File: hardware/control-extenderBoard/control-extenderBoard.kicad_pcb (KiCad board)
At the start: 2 copper layers, 100 x 135 mm, 88 parts, among them J1 12V + GND (TP), J10 SCL6 + GND (TP), J11 SDA6 + GND (TP), J12 3V3 + GND (TP), J13 12V + GND (TP), J14 SCL6 + GND (TP), J15 SDA6 + GND (TP), J17 24V IN, J18 GND, J2 12V Out, J3 5V out, J4 3V3 + GND (TP), J5 GND, J6 SCL7 Differential (TP), J7 SDA7 Differential (TP), J8 RS485, J9 3V3 out, P1 ISP, U1 MAX3485, U10 LM2576T-12, U11 ICM-426XX_Breakout, U2 PCA9600D, U3 TCA9548A_1-to-8_I2C_Multiplex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, U4 LM2576T-3.3, U5 PCA9600D, U6 PCA82C251, U7 PCA82C251, U8 PCA9600D, U9 LM2576T-5

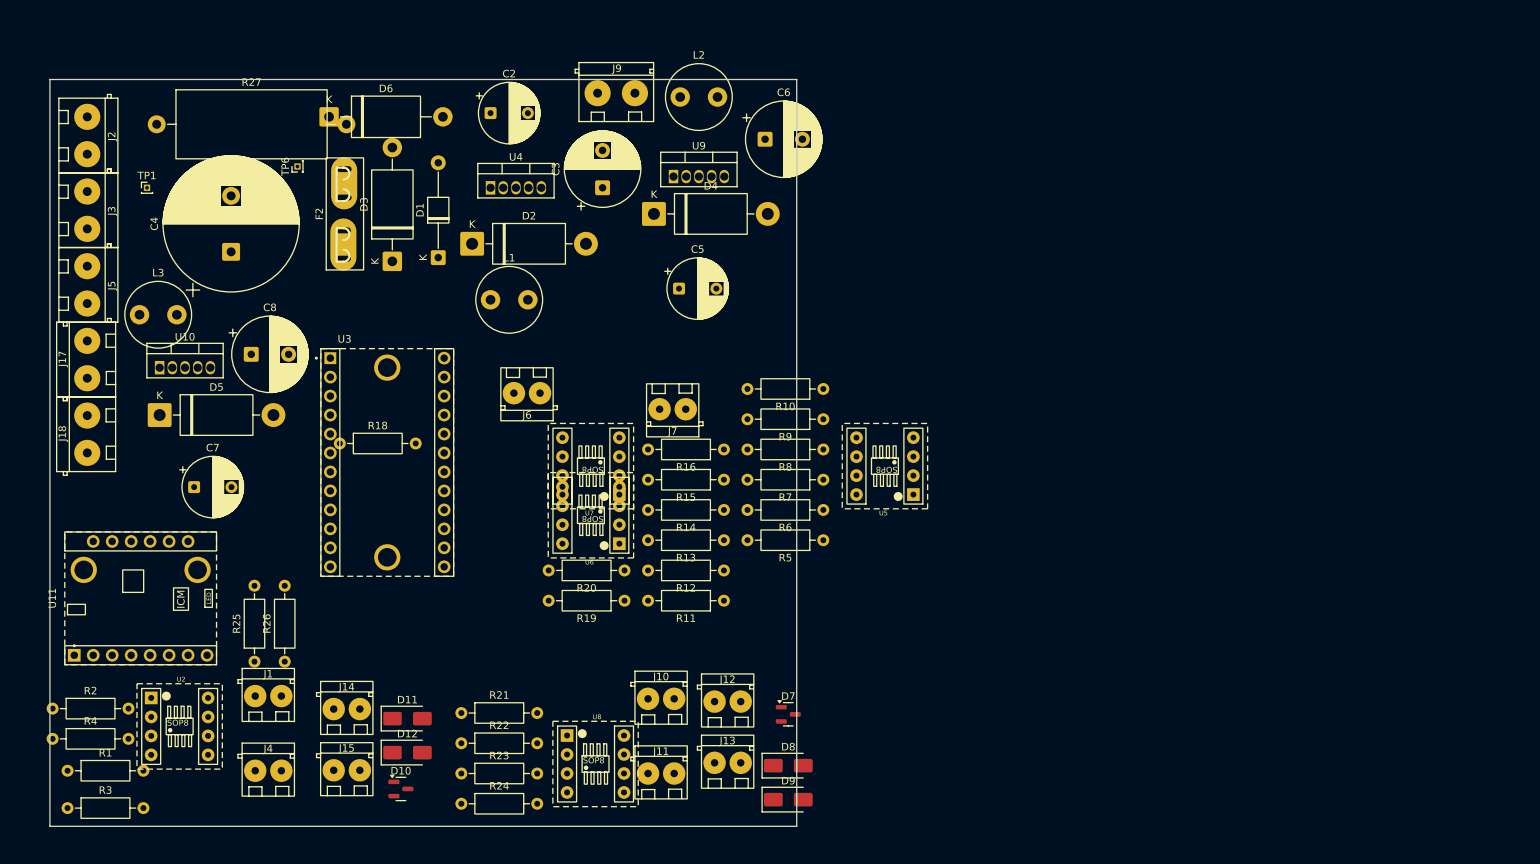
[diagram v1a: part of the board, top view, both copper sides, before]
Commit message: extenderBoard: Add remote encoder board, start arranging
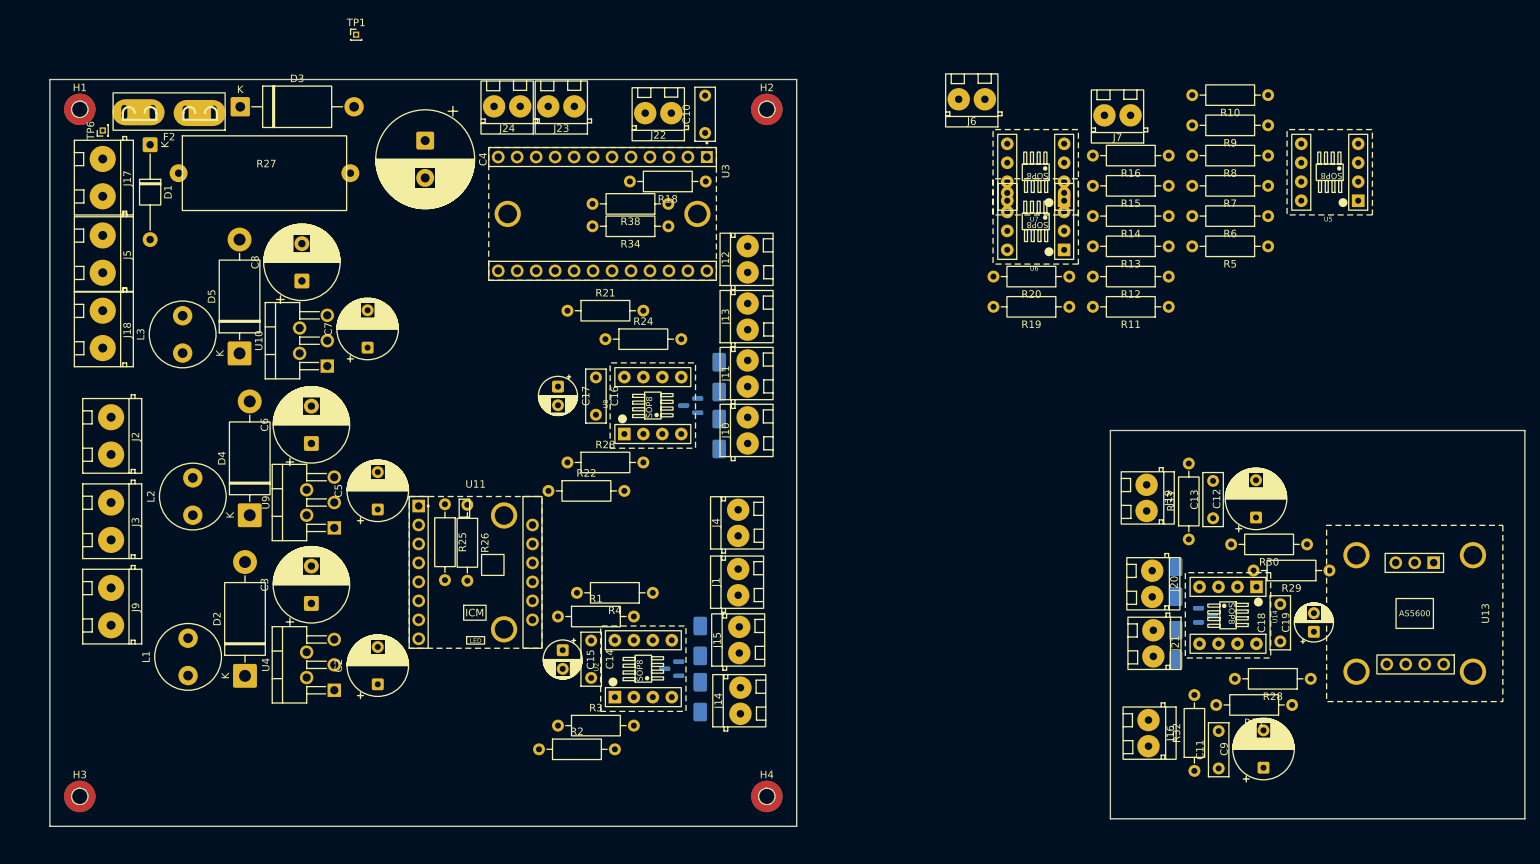
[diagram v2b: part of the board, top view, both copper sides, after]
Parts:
- removed D6: TVS 40V, Diode_THT:D_DO-201AE_P15.24mm_Horizontal
- added C10: 100n, Capacitor_THT:C_Disc_D7.0mm_W2.5mm_P5.00mm, F.Cu at (132.7, 37.2)
- added C11: 100n, Capacitor_THT:C_Disc_D7.0mm_W2.5mm_P5.00mm, F.Cu at (201.5, 122.2)
- added C12: 100u, Capacitor_THT:CP_Radial_D8.0mm_P5.00mm, F.Cu at (206.5, 88.7)
- added C13: 100n, Capacitor_THT:C_Disc_D7.0mm_W2.5mm_P5.00mm, F.Cu at (200.8, 88.8)
- added C14: 100n, Capacitor_THT:C_Disc_D7.0mm_W2.5mm_P5.00mm, F.Cu at (117.5, 105.1)
- added C15: 10uf, Capacitor_THT:CP_Radial_D5.0mm_P2.50mm, F.Cu at (113.7, 106.4)
- added C16: 100n, Capacitor_THT:C_Disc_D7.0mm_W2.5mm_P5.00mm, F.Cu at (118.1, 69.9)
- added C17: 10uf, Capacitor_THT:CP_Radial_D5.0mm_P2.50mm, F.Cu at (113.0, 71.1)
- added C18: 100n, Capacitor_THT:C_Disc_D7.0mm_W2.5mm_P5.00mm, F.Cu at (209.8, 105.2)
- added C19: 10uf, Capacitor_THT:CP_Radial_D5.0mm_P2.50mm, F.Cu at (214.2, 104.0)
- added C9: 100u, Capacitor_THT:CP_Radial_D8.0mm_P5.00mm, F.Cu at (207.5, 122.2)
- added D14: BAT54A, Package_TO_SOT_SMD:SOT-23, B.Cu at (199.8, 101.8)
- added D15: SMAJ150A, Diode_SMD:D_SMA, B.Cu at (195.8, 105.8)
- added D16: SMAJ150A, Diode_SMD:D_SMA, B.Cu at (195.8, 97.2)
- added H1: MountingHole_Pad, mountingHoles_libJonny:MountingHole_2.2mm_NPTH-with-pad_DRC-clearance-error, F.Cu at (49.0, 34.0)
- added H2: MountingHole_Pad, mountingHoles_libJonny:MountingHole_2.2mm_NPTH-with-pad_DRC-clearance-error, F.Cu at (141.0, 34.0)
- added H3: MountingHole_Pad, mountingHoles_libJonny:MountingHole_2.2mm_NPTH-with-pad_DRC-clearance-error, F.Cu at (49.0, 126.0)
- added H4: MountingHole_Pad, mountingHoles_libJonny:MountingHole_2.2mm_NPTH-with-pad_DRC-clearance-error, F.Cu at (141.0, 126.0)
- added J16: 12V + GND (TP), terminals_libJonny:ScrewTerminal_P3.5mm_2Pin_FP7x7, F.Cu at (192.1, 115.8)
- added J19: 3V3 + GND (TP), terminals_libJonny:ScrewTerminal_P3.5mm_2Pin_FP7x7, F.Cu at (191.8, 84.3)
- added J20: SCL6 + GND (TP), terminals_libJonny:ScrewTerminal_P3.5mm_2Pin_FP7x7, F.Cu at (192.6, 95.8)
- added J21: SDA6 + GND (TP), terminals_libJonny:ScrewTerminal_P3.5mm_2Pin_FP7x7, F.Cu at (192.8, 103.8)
- added J22: SDA, SCL - ESP32, terminals_libJonny:ScrewTerminal_P3.5mm_2Pin_FP7x7, F.Cu at (128.2, 34.5)
- added J23: I2C Reserve, terminals_libJonny:ScrewTerminal_P3.5mm_2Pin_FP7x7, F.Cu at (115.2, 33.6)
- added J24: I2C Reserve, terminals_libJonny:ScrewTerminal_P3.5mm_2Pin_FP7x7, F.Cu at (108.0, 33.6)
- added R28: 2k2, Resistor_THT:R_Axial_DIN0207_L6.3mm_D2.5mm_P10.16mm_Horizontal, F.Cu at (213.8, 110.2)
- added R29: 2k2, Resistor_THT:R_Axial_DIN0207_L6.3mm_D2.5mm_P10.16mm_Horizontal, F.Cu at (216.3, 95.8)
- added R30: 750, Resistor_THT:R_Axial_DIN0207_L6.3mm_D2.5mm_P10.16mm_Horizontal, F.Cu at (213.3, 92.2)
- added R31: 750, Resistor_THT:R_Axial_DIN0207_L6.3mm_D2.5mm_P10.16mm_Horizontal, F.Cu at (211.3, 113.8)
- added R32: 10, Resistor_THT:R_Axial_DIN0207_L6.3mm_D2.5mm_P10.16mm_Horizontal, F.Cu at (198.2, 122.6)
- added R33: 10, Resistor_THT:R_Axial_DIN0207_L6.3mm_D2.5mm_P10.16mm_Horizontal, F.Cu at (197.5, 91.6)
- added R34: 2k2, Resistor_THT:R_Axial_DIN0207_L6.3mm_D2.5mm_P10.16mm_Horizontal, F.Cu at (127.8, 49.7)
- added R38: 2k2, Resistor_THT:R_Axial_DIN0207_L6.3mm_D2.5mm_P10.16mm_Horizontal, F.Cu at (127.8, 46.7)
- added U13: AS5600_Breakout, modules_libJonny:AS5600_Magnetic-Encoder_Breakout_Board, F.Cu at (227.8, 101.5)
- added U14: PCA9600D, modules_libJonny:Adapter-Board_SOP8_to_DIP8, F.Cu at (202.8, 101.8)
- C4: footprint Capacitor_THT:CP_Radial_D18.0mm_P7.50mm -> Capacitor_THT:CP_Radial_D13.0mm_P5.00mm
- D10, D11, D12, D7, D8, D9: moved to B.Cu
- R27: footprint Resistor_THT:R_Axial_DIN0922_L20.0mm_D9.0mm_P25.40mm_Horizontal -> resistors_libJonny:Cement-Power-R_L22_W10_P23_Horizontal
- U10, U4, U9: footprint Package_TO_SOT_THT:TO-220-5_Vertical -> Package_TO_SOT_THT:TO-220-5_P3.4x3.7mm_StaggerOdd_Lead3.8mm_Vertical
- moved J9 92.9 mm to (53.2, 98.1), turned to -90 degrees
- moved L2 86.0 mm to (64.1, 88.3), turned to 90 degrees
- moved R4 82.7 mm to (125.7, 98.7), turned to 180 degrees
- moved C2 78.0 mm to (88.9, 111.0), turned to 90 degrees
- moved C6 73.1 mm to (80.0, 78.7), turned to 90 degrees
- moved J4 71.9 mm to (137.2, 91.1), turned to 90 degrees
- moved J6 71.4 mm to (170.2, 32.6)
- moved J7 71.4 mm to (189.7, 34.8)
- moved R10 71.4 mm to (208.1, 32.1)
- moved R11 71.4 mm to (194.8, 60.4)
- moved R12 71.4 mm to (194.8, 56.4)
- moved R13 71.4 mm to (194.8, 52.3)
- moved R14 71.4 mm to (194.8, 48.3)
- moved R15 71.4 mm to (194.8, 44.2)
- moved R16 71.4 mm to (194.8, 40.2)
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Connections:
- C1 pad 2: GNDPWR -> GND
- C2 pad 2: +24V filtered -> GND
- C3 pad 2: +24V filtered -> GND
- C4 pad 2: +24V filtered -> GND
- C5 pad 2: +24V filtered -> GND
- C6 pad 2: +24V filtered -> GND
- C7 pad 2: +24V filtered -> GND
- C8 pad 2: +24V filtered -> GND
- D1 pad 2: +24V filtered -> GND
- D10 pad 3: +24V filtered -> GND
- D11 pad 2: +24V filtered -> GND
- D12 pad 2: +24V filtered -> GND
- D13 pad 3: +24V filtered -> GND
- D2 pad 2: +24V filtered -> GND
- D3 pad 1: +24V filtered -> GND
- D4 pad 2: +24V filtered -> GND
- D5 pad 2: +24V filtered -> GND
- D7 pad 3: +24V filtered -> GND
- D8 pad 2: +24V filtered -> GND
- D9 pad 2: +24V filtered -> GND
- J1 pad 2: +24V filtered -> GND
- J10 pad 1: +24V filtered -> GND
- J11 pad 1: +24V filtered -> GND
- J12 pad 2: +24V filtered -> GND
- J13 pad 2: +24V filtered -> GND
- J14 pad 1: +24V filtered -> GND
- J15 pad 1: +24V filtered -> GND
- J18 pad 1: +24V filtered -> GND
- J18 pad 2: +24V filtered -> GND
- J4 pad 2: +24V filtered -> GND
- J5 pad 1: +24V filtered -> GND
- J5 pad 2: +24V filtered -> GND
- J8 pad 1: +24V filtered -> GND
- R12 pad 2: +24V filtered -> GND
- R21 pad 2: /I2C5_SDA -> /I2C4_SDA
- R22 pad 2: /I2C5_SCL -> /I2C4_SCL
- R37 pad 2: +24V filtered -> GND
- R5 pad 2: +24V filtered -> GND
- R6 pad 2: +24V filtered -> GND
- R9 pad 2: +24V filtered -> GND
- U1 pad 5: +24V filtered -> GND
- U10 pad 3: +24V filtered -> GND
- U10 pad 5: +24V filtered -> GND
- U11 pad 2: +24V filtered -> GND
- U2 pad 4: +24V filtered -> GND
- U3 pad 2: +24V filtered -> GND
- U3 pad 6: +24V filtered -> GND
- U3 pad 7: +24V filtered -> GND
- U3 pad 8: +24V filtered -> GND
- U4 pad 3: +24V filtered -> GND
- U4 pad 5: +24V filtered -> GND
- U5 pad 4: +24V filtered -> GND
- U6 pad 2: +24V filtered -> GND
- U7 pad 2: +24V filtered -> GND
- U8 pad 1: /I2C5_SCL -> /I2C4_SCL
- U8 pad 4: +24V filtered -> GND
- U8 pad 7: /I2C5_SDA -> /I2C4_SDA
- U9 pad 3: +24V filtered -> GND
- U9 pad 5: +24V filtered -> GND
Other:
- board size 100 x 135 mm -> 197.5 x 135 mm
- copper layers 2 -> 4

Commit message: extenderBoard: Evaluate part availability, Rework i2c protection
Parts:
- removed U11: ICM-426XX_Breakout, modules_libJonny:ICM-426XX_6-Axis-Gyro_Breakout_Board
- added D17: AQ4020-01FTG, Diode_SMD:D_SOD-323_HandSoldering, B.Cu at (85.2, 122.6)
- added D18: AQ4020-01FTG, Diode_SMD:D_SOD-323_HandSoldering, B.Cu at (101.5, 122.4)
- added D19: BAS70-04, Package_TO_SOT_SMD:SOT-23-3, B.Cu at (107.0, 118.9)
- added D20: AQ4020-01FTG, Diode_SMD:D_SOD-323_HandSoldering, B.Cu at (93.2, 122.3)
- added D21: BAS70-04, Package_TO_SOT_SMD:SOT-23-3, B.Cu at (131.4, 112.4)
- added D22: BAS70-04, Package_TO_SOT_SMD:SOT-23-3, B.Cu at (128.0, 114.8)
- added D23: BAS70-04, Package_TO_SOT_SMD:SOT-23-3, B.Cu at (99.5, 118.6)
- added D24: BAS70-04, Package_TO_SOT_SMD:SOT-23-3, B.Cu at (93.0, 119.0)
- added D25: BAS70-04, Package_TO_SOT_SMD:SOT-23-3, B.Cu at (83.2, 119.3)
- added D26: BAS70-04, Package_TO_SOT_SMD:SOT-23-3, F.Cu at (219.8, 121.5)
- added D6: AQ4020-01FTG, Diode_SMD:D_SOD-323_HandSoldering, B.Cu at (109.5, 122.4)
- added J25: I2C Reserve SDA/GND, terminals_libJonny:ScrewTerminal_P3.5mm_2Pin_FP7x7, F.Cu at (107.2, 125.8)
- added J26: I2C Reserve SDA/GND, terminals_libJonny:ScrewTerminal_P3.5mm_2Pin_FP7x7, F.Cu at (91.2, 125.7)
- added R39: 2k2, Resistor_THT:R_Axial_DIN0207_L6.3mm_D2.5mm_P10.16mm_Horizontal, F.Cu at (122.5, 6.00)
- added R40: 2k2, Resistor_THT:R_Axial_DIN0207_L6.3mm_D2.5mm_P10.16mm_Horizontal, F.Cu at (118.0, 93.7)
- added R41: 2k2, Resistor_THT:R_Axial_DIN0207_L6.3mm_D2.5mm_P10.16mm_Horizontal, F.Cu at (122.6, 85.0)
- added R42: 2k2, Resistor_THT:R_Axial_DIN0207_L6.3mm_D2.5mm_P10.16mm_Horizontal, F.Cu at (91.7, 114.6)
- added a1: ICM-426XX_Breakout, modules_libJonny:ICM-426XX_6-Axis-Gyro_Breakout_Board, F.Cu at (65.7, 120.0)
- C9: footprint Capacitor_THT:CP_Radial_D8.0mm_P5.00mm -> Capacitor_THT:CP_Radial_D6.3mm_P2.50mm
- D10, D14, D7: value BAT54A -> BAS70-04; footprint Package_TO_SOT_SMD:SOT-23 -> Package_TO_SOT_SMD:SOT-23-3
- D11, D12, D15, D16, D8, D9: value SMAJ150A -> SMF12VTR; footprint Diode_SMD:D_SMA -> Diode_SMD:D_SOD-123F
- J23, J24: value I2C Reserve -> I2C Reserve SCL/GND
- L1: value 100u -> 150u; footprint Inductor_THT:L_Radial_D8.7mm_P5.00mm_Fastron_07HCP -> Inductor_THT:L_Radial_D12.5mm_P7.00mm_Fastron_09HCP
- L2: value 100u -> 330u; footprint Inductor_THT:L_Radial_D8.7mm_P5.00mm_Fastron_07HCP -> Inductor_THT:L_Radial_D10.5mm_P5.00mm_Abacron_AISR-01
- L3: value 100u -> 470u; footprint Inductor_THT:L_Radial_D8.7mm_P5.00mm_Fastron_07HCP -> Inductor_THT:L_Toroid_Vertical_L21.6mm_W11.4mm_P7.62mm_Pulse_KM-3
- moved J24 95.3 mm to (83.4, 125.7), turned to 0 degrees
- moved J23 93.5 mm to (99.5, 125.8), turned to 0 degrees
- moved J22 92.2 mm to (117.1, 126.0), turned to 0 degrees
- moved C10 64.8 mm to (101.6, 93.9)
- moved R18 57.4 mm to (105.0, 93.8), turned to 0 degrees
- moved R26 52.5 mm to (60.6, 120.6), turned to 0 degrees
- moved R25 52.4 mm to (60.5, 123.6), turned to 0 degrees
- moved R38 47.6 mm to (110.0, 90.8), turned to 0 degrees
- moved R34 42.1 mm to (110.0, 87.8), turned to 0 degrees
- moved D10 41.9 mm to (128.0, 67.0), turned to -90 degrees
- moved U3 41.5 mm to (118.8, 89.5), turned to 90 degrees
- moved L1 25.5 mm to (84.8, 95.8), turned to 180 degrees
- moved J12 23.7 mm to (139.8, 79.5)
- moved J13 23.7 mm to (139.8, 87.2)
- moved J6 16.5 mm to (186.7, 32.0)
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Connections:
- D10 pad 1: Net-(D11-A1) -> GND
- D10 pad 2: Net-(D12-A1) -> +12V
- D10 pad 3: GND -> /SCL_Boost2
- D11 pad 1: Net-(D11-A1) -> /SDA_Boost1
- D12 pad 1: Net-(D12-A1) -> /SCL_Boost1
- D14 pad 1: /Remote-I2C-Sensor-Board/SDA_REMOTE-IN -> GND_REMOTE
- D14 pad 2: /Remote-I2C-Sensor-Board/SCL_REMOTE-IN -> +12V_REMOTE
- D14 pad 3: GND_REMOTE -> /Remote-I2C-Sensor-Board/SDA_REMOTE-IN
- D15 pad 1: /Remote-I2C-Sensor-Board/SDA_REMOTE-IN -> /Remote-I2C-Sensor-Board/SCL_REMOTE-IN
- D16 pad 1: /Remote-I2C-Sensor-Board/SCL_REMOTE-IN -> /Remote-I2C-Sensor-Board/SDA_REMOTE-IN
- D7 pad 1: Net-(D9-A1) -> GND
- D7 pad 2: Net-(D8-A1) -> +12V
- D7 pad 3: GND -> /SDA_Boost2
- D8 pad 1: Net-(D8-A1) -> /SCL_Boost2
- D9 pad 1: Net-(D9-A1) -> /SDA_Boost2
- J10 pad 2: Net-(D8-A1) -> /SCL_Boost2
- J11 pad 2: Net-(D9-A1) -> /SDA_Boost2
- J14 pad 2: Net-(D12-A1) -> /SCL_Boost1
- J15 pad 2: Net-(D11-A1) -> /SDA_Boost1
- J23 pad 2: /I2C1_SDA -> GND
- J24 pad 2: /I2C2_SDA -> GND
- R23 pad 2: Net-(D8-A1) -> /SCL_Boost2
- R24 pad 2: Net-(D9-A1) -> /SDA_Boost2
- R3 pad 2: Net-(D12-A1) -> /SCL_Boost1
- R4 pad 2: Net-(D11-A1) -> /SDA_Boost1
- U2 pad 2: Net-(D12-A1) -> /SCL_Boost1
- U2 pad 3: Net-(D12-A1) -> /SCL_Boost1
- U2 pad 5: Net-(D11-A1) -> /SDA_Boost1
- U2 pad 6: Net-(D11-A1) -> /SDA_Boost1
- U8 pad 2: Net-(D8-A1) -> /SCL_Boost2
- U8 pad 3: Net-(D8-A1) -> /SCL_Boost2
- U8 pad 5: Net-(D9-A1) -> /SDA_Boost2
- U8 pad 6: Net-(D9-A1) -> /SDA_Boost2
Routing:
- net /SCL_Boost1: track 0.00 -> 18.8 mm
- net GND: track 0.00 -> 15.8 mm
- net /SDA_Boost1: track 0.00 -> 15.4 mm
- net +12V: track 0.00 -> 8.02 mm

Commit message: extenderBoard: I2C add series Resistors, Add CAT6 Shield, Chassis GND, Arrange vertical R footprints
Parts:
- added C20: 100n, Capacitor_THT:C_Disc_D7.0mm_W2.5mm_P5.00mm, F.Cu at (129.0, 40.5)
- added J27: CAT6-Shield, misc_libJonny:Shield_Landing_Pad_6mmCable_ZipTie, F.Cu at (148.5, 46.5)
- added J28: CAT6-Shield, misc_libJonny:Shield_Landing_Pad_6mmCable_ZipTie, F.Cu at (156.5, 80.5)
- added J29: Chassis, terminals_libJonny:ScrewTerminal_P5mm_2Pin_FP10x8, F.Cu at (135.8, 33.9)
- added R43: 1M, Resistor_THT:R_Axial_DIN0207_L6.3mm_D2.5mm_P10.16mm_Horizontal, F.Cu at (138.1, 43.5)
- added R44: 22, Resistor_THT:R_Axial_DIN0207_L6.3mm_D2.5mm_P10.16mm_Horizontal, F.Cu at (97.0, 120.1)
- added R45: 22, Resistor_THT:R_Axial_DIN0207_L6.3mm_D2.5mm_P10.16mm_Horizontal, F.Cu at (105.0, 120.1)
- added R46: 22, Resistor_THT:R_Axial_DIN0207_L6.3mm_D2.5mm_P10.16mm_Horizontal, F.Cu at (81.0, 120.6)
- added R47: 22, Resistor_THT:R_Axial_DIN0207_L6.3mm_D2.5mm_P10.16mm_Horizontal, F.Cu at (89.0, 120.1)
- added R48: 22, Resistor_THT:R_Axial_DIN0207_L6.3mm_D2.5mm_P10.16mm_Horizontal, F.Cu at (124.7, 78.2)
- added R49: 22, Resistor_THT:R_Axial_DIN0207_L6.3mm_D2.5mm_P10.16mm_Horizontal, F.Cu at (124.7, 88.5)
- R34, R38, R39, R40, R41, R42: footprint Resistor_THT:R_Axial_DIN0207_L6.3mm_D2.5mm_P10.16mm_Horizontal -> Resistor_THT:R_Axial_DIN0207_L6.3mm_D2.5mm_P2.54mm_Vertical
- moved J6 237.8 mm to (-23.8, 142.7)
- moved J7 237.8 mm to (-4.30, 144.8)
- moved R10 237.8 mm to (14.1, 142.1)
- moved R11 237.8 mm to (0.81, 170.4)
- moved R12 237.8 mm to (0.81, 166.4)
- moved R13 237.8 mm to (0.81, 162.3)
- moved R14 237.8 mm to (0.81, 158.3)
- moved R15 237.8 mm to (0.81, 154.2)
- moved R16 237.8 mm to (0.81, 150.2)
- moved R19 237.8 mm to (-12.5, 170.4)
- moved R20 237.8 mm to (-12.5, 166.4)
- moved R5 237.8 mm to (14.1, 162.3)
- moved R6 237.8 mm to (14.1, 158.3)
- moved R7 237.8 mm to (14.1, 154.2)
- moved R8 237.8 mm to (14.1, 150.2)
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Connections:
- D17 pad 1: /I2C2_SCL -> Net-(D17-A1)
- D18 pad 1: /I2C1_SCL -> Net-(D18-A1)
- D20 pad 1: /I2C2_SDA -> Net-(D20-A1)
- D6 pad 1: /I2C1_SDA -> Net-(D6-A1)
- J22 pad 1: /I2C_MASTER_SDA -> /ESP32_SDA
- J22 pad 2: /I2C_MASTER_SCL -> /ESP32_SCL
- J23 pad 1: /I2C1_SCL -> Net-(D18-A1)
- J24 pad 1: /I2C2_SCL -> Net-(D17-A1)
- J25 pad 1: /I2C1_SDA -> Net-(D6-A1)
- J26 pad 1: /I2C2_SDA -> Net-(D20-A1)
- R1 pad 2: /I2C5_SDA -> /I2C0_SDA
- R2 pad 2: /I2C5_SCL -> /I2C0_SCL
- R21 pad 2: /I2C4_SDA -> /I2C1_SDA
- R22 pad 2: /I2C4_SCL -> /I2C1_SCL
- R34 pad 2: /I2C_MASTER_SDA -> /ESP32_SDA
- R38 pad 2: /I2C_MASTER_SCL -> /ESP32_SCL
- R39 pad 2: /I2C1_SCL -> Net-(D18-A1)
- R40 pad 2: /I2C1_SDA -> Net-(D6-A1)
- R41 pad 2: /I2C2_SCL -> Net-(D17-A1)
- R42 pad 2: /I2C2_SDA -> Net-(D20-A1)
- U2 pad 1: /I2C5_SCL -> /I2C0_SCL
- U2 pad 7: /I2C5_SDA -> /I2C0_SDA
- U3 pad 3: /I2C_MASTER_SDA -> /MASTER_SDA
- U3 pad 4: /I2C_MASTER_SCL -> /MASTER_SCL
- U8 pad 1: /I2C4_SCL -> /I2C1_SCL
- U8 pad 7: /I2C4_SDA -> /I2C1_SDA
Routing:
- net /I2C0_SCL: track 0.00 -> 55.7 mm
- net /I2C0_SDA: track 0.00 -> 46.7 mm
- net /I2C1_SDA: track 0.00 -> 32.2 mm
- net GND: track 15.8 -> 42.6 mm
- net /I2C1_SCL: track 0.00 -> 17.3 mm
- net /MASTER_SCL: track 0.00 -> 13.4 mm
- net +12V: track 8.02 -> 18.0 mm
- net /ESP32_SCL: track 0.00 -> 8.84 mm
- net /ESP32_SDA: track 0.00 -> 8.59 mm
- net /MASTER_SDA: track 0.00 -> 6.63 mm
- net +3V3: track 0.00 -> 3.50 mm
- net /SCL_Boost1: track 18.8 -> 17.8 mm
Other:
- outline, holes or cut-outs redrawn
